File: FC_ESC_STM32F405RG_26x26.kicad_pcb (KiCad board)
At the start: 2 copper layers, 34 x 34 mm, 223 parts, among them J1 USB, J10 UART4, J11 PWM, J12 OSD, J13 ALARM, J14 LED_STRIP, J15 RC, J16 MOTOR, J17 MOTOR, J18 MOTOR, J19 MOTOR, J2 ESC_PROG, J21 Conn_02x03_Odd_Even, J22 Conn_02x02_Odd_Even, J3 Debugger, J4 VOL_CUR, J5 RSSI, J6 I2C2_UART3, J7 SD CARD, J8 UART1, J9 UART6, Q1 SIZ200, Q10 SIZ200, Q11 SIZ200, Q12 SIZ200, Q2 SIZ200, Q3 SIZ200, Q4 SIZ200, Q5 SIZ200, Q6 SIZ200, Q7 SIZ200, Q8 SIZ200, Q9 SIZ200, SW1 RST, U1 EFM8BB21, U10 FD6288Q, U11 outline, U12 MPU-6000, U13 BMP280, U14 LM358, U15 STM32F405RGTx, U16 TPS54331D, U2 EFM8BB21, U3 TPS54560BDDA, U4 FD6288Q, U5 FD6288Q, U7 EFM8BB21, U8 EFM8BB21, U9 FD6288Q, Y1 8MHz

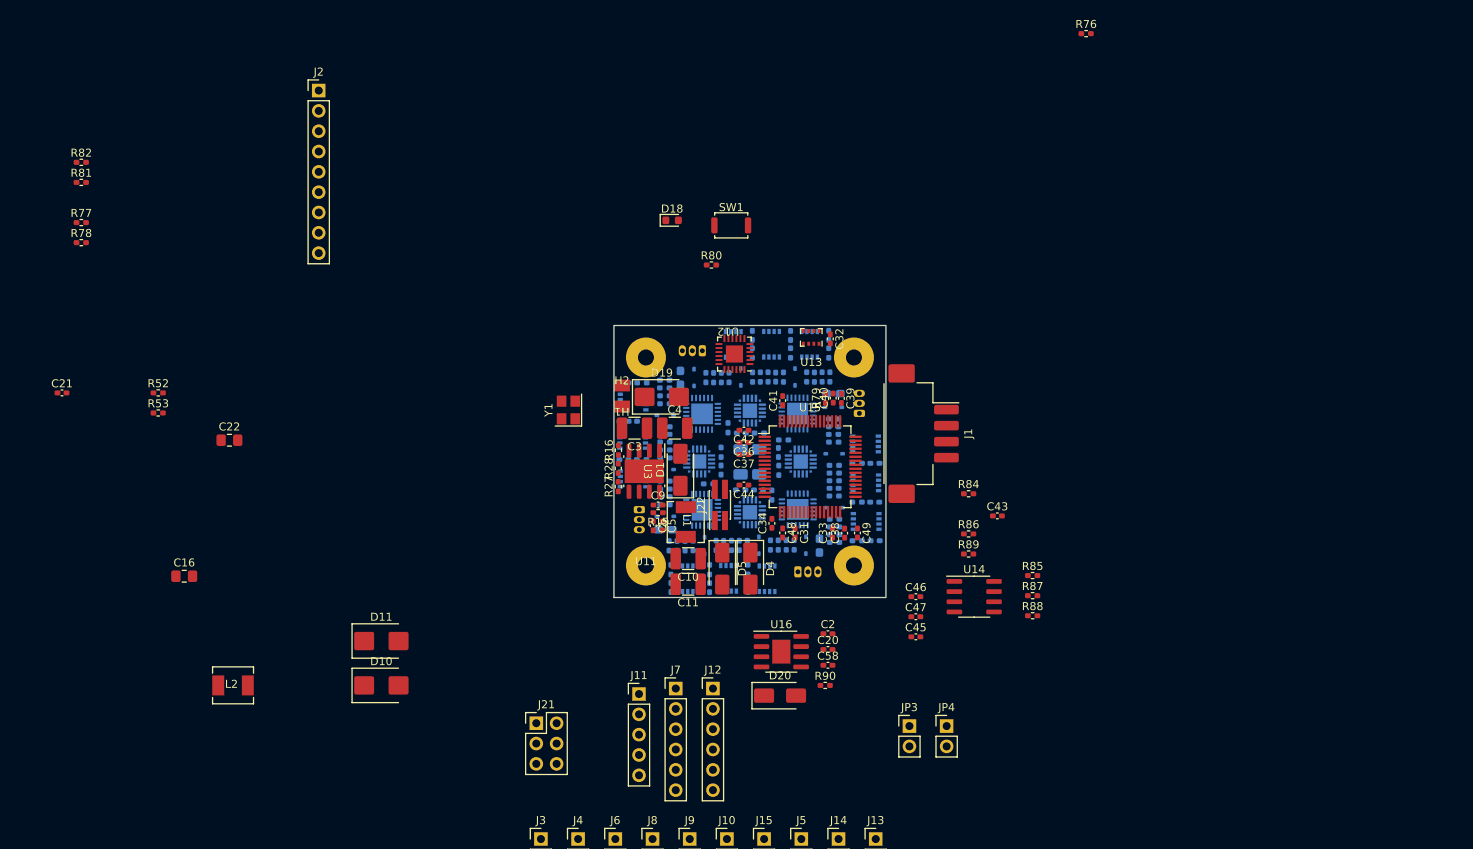
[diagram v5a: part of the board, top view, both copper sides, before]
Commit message: update placement
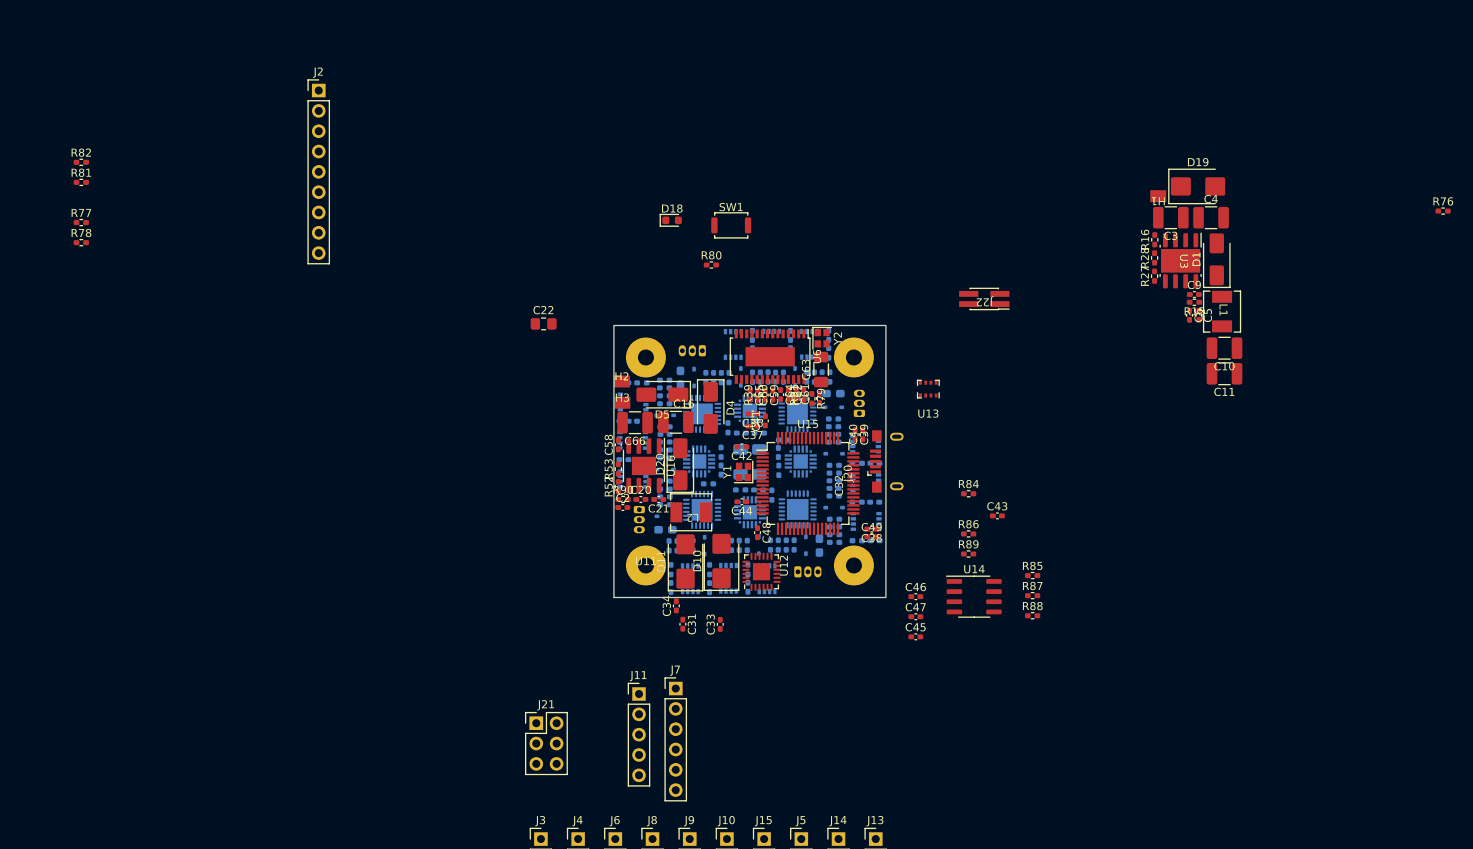
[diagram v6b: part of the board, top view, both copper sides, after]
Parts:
- removed J1: USB, Connector_Hirose:Hirose_DF3EA-04P-2H_1x04-1MP_P2.00mm_Horizontal
- removed J12: OSD, Connector_PinHeader_2.54mm:PinHeader_1x06_P2.54mm_Vertical
- removed JP3: Jumper_3V3_FC, Connector_PinHeader_2.54mm:PinHeader_1x02_P2.54mm_Vertical
- removed JP4: Jumper_3V3_ESC, Connector_PinHeader_2.54mm:PinHeader_1x02_P2.54mm_Vertical
- added C59: 100nF, Capacitor_SMD:C_0402_1005Metric_Pad0.74x0.62mm_HandSolder, F.Cu at (217.5, 71.9)
- added C60: 100nF, Capacitor_SMD:C_0402_1005Metric_Pad0.74x0.62mm_HandSolder, F.Cu at (218.4, 71.9)
- added C61: 47uF, Capacitor_SMD:C_0402_1005Metric_Pad0.74x0.62mm_HandSolder, F.Cu at (221.3, 71.8)
- added C62: 22uF, Capacitor_SMD:C_0402_1005Metric_Pad0.74x0.62mm_HandSolder, F.Cu at (220.4, 71.9)
- added C63: 4.7uF, Capacitor_SMD:C_1206_3216Metric_Pad1.33x1.80mm_HandSolder, F.Cu at (224.5, 68.7)
- added C64: 100nF, Capacitor_SMD:C_0402_1005Metric_Pad0.74x0.62mm_HandSolder, F.Cu at (219.4, 71.9)
- added C65: 100nF, Capacitor_SMD:C_0402_1005Metric_Pad0.74x0.62mm_HandSolder, F.Cu at (215.6, 71.9)
- added C66: 10uF, Capacitor_SMD:C_1210_3225Metric_Pad1.33x2.70mm_HandSolder, F.Cu at (201.2, 75.4)
- added H3: Pad_5V_IN, Proj_footprint:MoutingPad, F.Cu at (199.6, 72.9)
- added J20: USB_A, Proj_footprint:USB_Micro-B_2P_4hole, F.Cu at (236.1, 80.2)
- added R39: 75R, Resistor_SMD:R_0402_1005Metric_Pad0.72x0.64mm_HandSolder, F.Cu at (216.5, 71.9)
- added R91: 75R, Resistor_SMD:R_0402_1005Metric_Pad0.72x0.64mm_HandSolder, F.Cu at (222.3, 71.9)
- added U6: AT7456, Package_SO:TSSOP-28-1EP_4.4x9.7mm_P0.65mm, F.Cu at (218.1, 67.1)
- added Y2: 8Mhz, Crystal:Crystal_SMD_2016-4Pin_2.0x1.6mm, F.Cu at (224.6, 64.8)
- C16: footprint Capacitor_SMD:C_0805_2012Metric_Pad1.18x1.45mm_HandSolder -> Capacitor_SMD:C_1210_3225Metric_Pad1.33x2.70mm_HandSolder
- J22: footprint Connector_PinHeader_1.27mm:PinHeader_2x02_P1.27mm_Vertical_SMD -> Proj_footprint:PinHeader_2x02_P1.27mm_Vertical_SMD
- Y1: footprint Crystal:Crystal_SMD_3225-4Pin_3.2x2.5mm -> Crystal:Crystal_SMD_2016-4Pin_2.0x1.6mm
- moved C21 75.8 mm to (204.2, 85.0), turned to 180 degrees
- moved D1 72.0 mm to (273.9, 55.0)
- moved H1 72.0 mm to (266.6, 47.1)
- moved R27 72.0 mm to (266.1, 57.1)
- moved R28 72.0 mm to (266.1, 54.8)
- moved C10 72.0 mm to (274.9, 66.1)
- moved C11 72.0 mm to (274.9, 69.3)
- moved C3 72.0 mm to (268.2, 49.8)
- moved C4 72.0 mm to (273.2, 49.8)
- moved C5 72.0 mm to (271.7, 62.0)
- moved L1 72.0 mm to (274.6, 61.5)
- moved R16 72.0 mm to (266.2, 52.5)
- moved U3 72.0 mm to (269.4, 55.1)
- moved C6 72.0 mm to (270.5, 62.0)
- moved D19 72.0 mm to (271.6, 45.9)
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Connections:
- net BARO_CLK renamed SPI3_CLK
- net BARO_MISO renamed SPI3_MISO
- net BARO_MOSI renamed SPI3_MOSI
- C16 pad 1: Net-(J22-Pin_4) -> +5V
- D4 pad 1: Net-(D4-K) -> +5V
- D5 pad 1: Net-(D4-K) -> +5V
- J22 pad 1: Net-(D4-K) -> Net-(D10-K)
- J22 pad 2: +5V -> 3V3_FC
- J22 pad 3: Net-(D4-K) -> Net-(D10-K)
- J22 pad 4: Net-(J22-Pin_4) -> 3V3_ESC
- U16 pad 2: Net-(J22-Pin_4) -> +5V

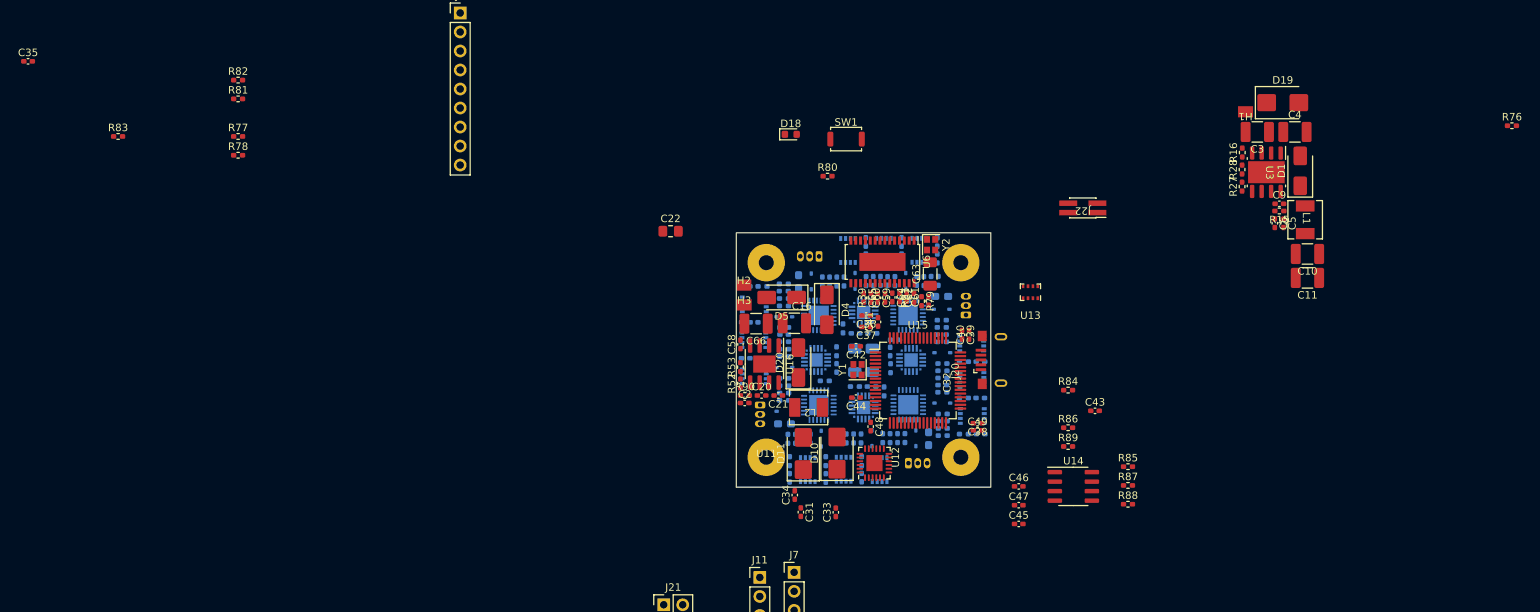
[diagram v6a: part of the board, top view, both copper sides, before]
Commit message: update placement
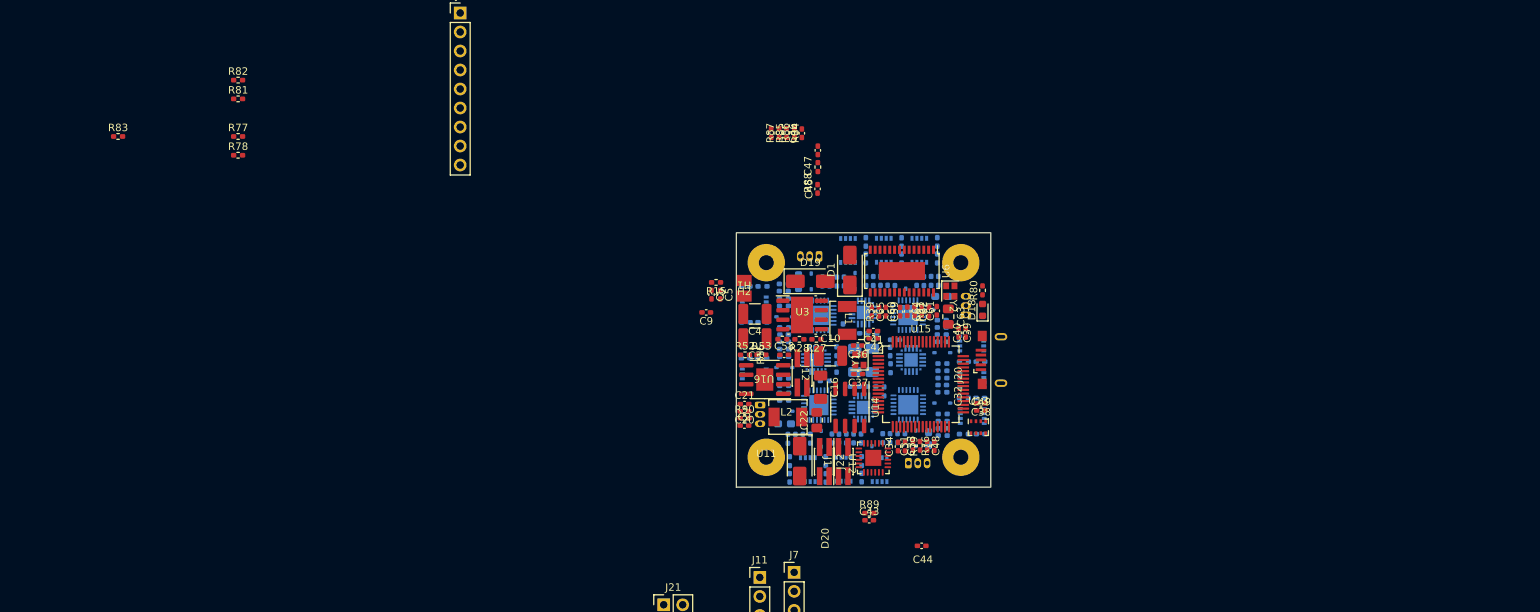
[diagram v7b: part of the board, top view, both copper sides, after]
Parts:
- removed C11, C66: 10uF, Capacitor_SMD:C_1210_3225Metric_Pad1.33x2.70mm_HandSolder
- removed C35: 100nF, Capacitor_SMD:C_0402_1005Metric_Pad0.74x0.62mm_HandSolder
- removed D10, D11: SS24, Diode_SMD:D_SMB
- removed D4, D5: SS34, Diode_SMD:D_SMA
- removed H3: Pad_5V_IN, Proj_footprint:MoutingPad
- removed SW1: RST, Button_Switch_SMD:SW_Push_SPST_NO_Alps_SKRK
- added J1: Conn_02x02_Odd_Even, Proj_footprint:PinHeader_2x02_P1.27mm_Vertical_SMD, F.Cu at (210.2, 93.8)
- added J12: Conn_02x02_Odd_Even, Proj_footprint:PinHeader_2x02_P1.27mm_Vertical_SMD, F.Cu at (207.3, 82.0)
- C16: footprint Capacitor_SMD:C_1210_3225Metric_Pad1.33x2.70mm_HandSolder -> Capacitor_SMD:C_1206_3216Metric_Pad1.33x1.80mm_HandSolder
- C4: value 10uF -> 100uF
- C63: footprint Capacitor_SMD:C_1206_3216Metric_Pad1.33x1.80mm_HandSolder -> Capacitor_SMD:C_0805_2012Metric_Pad1.18x1.45mm_HandSolder
- D19: value SS54 -> SS34; footprint Diode_SMD:D_SMB -> Diode_SMD:D_SMA
- U16: footprint Package_SO:SOIC-8-1EP_3.9x4.9mm_P1.27mm_EP2.29x3mm -> Proj_footprint:SOIC-8-1EP_3.9x4.9mm_P1.27mm_EP2.29x3mm
- Y1, Y2: footprint Crystal:Crystal_SMD_2016-4Pin_2.0x1.6mm -> Proj_footprint:Crystal_SMD_2016-4Pin_2.0x1.6mm
- moved R76 88.3 mm to (225.0, 91.7), turned to 90 degrees
- moved C9 77.9 mm to (194.5, 73.9), turned to 180 degrees
- moved C4 76.1 mm to (201.0, 74.1), turned to 180 degrees
- moved C5 75.9 mm to (196.4, 71.5)
- moved C6 75.9 mm to (195.2, 71.5)
- moved R15 75.9 mm to (195.8, 69.9)
- moved C3 72.6 mm to (201.0, 77.3)
- moved H1 70.7 mm to (199.6, 69.6)
- moved D19 67.5 mm to (208.4, 69.7)
- moved R16 66.3 mm to (204.7, 77.4), turned to 180 degrees
- moved R87 66.3 mm to (204.3, 49.9), turned to 90 degrees
- moved R85 65.3 mm to (203.2, 49.9), turned to -90 degrees
- moved C10 65.2 mm to (211.1, 79.7), turned to 0 degrees
- moved U3 64.9 mm to (207.3, 74.2), turned to 0 degrees
- moved R28 63.4 mm to (207.0, 77.5), turned to 180 degrees
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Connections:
- C1 pad 2: GND -> +5V
- C10 pad 1: Net-(D5-A) -> Net-(J12-Pin_3)
- C10 pad 2: GND -> +5V
- C16 pad 1: +5V -> Net-(J12-Pin_3)
- C16 pad 2: GND -> +5V
- C19 pad 2: GND -> +5V
- C2 pad 2: GND -> +5V
- C20 pad 2: GND -> +5V
- C22 pad 2: GND -> +5V
- C23 pad 2: GND -> +5V
- C24 pad 2: GND -> +5V
- C3 pad 2: GND -> +5V
- C31 pad 2: GND -> +5V
- C32 pad 2: GND -> +5V
- C33 pad 2: GND -> +5V
- C34 pad 2: GND -> +5V
- C36 pad 2: GND -> +5V
- C37 pad 2: GND -> +5V
- C38 pad 1: GND -> +5V
- C39 pad 1: GND -> +5V
- C4 pad 2: GND -> +5V
- C40 pad 2: GND -> +5V
- C41 pad 2: GND -> +5V
- C42 pad 2: GND -> +5V
- C43 pad 2: GND -> +5V
- C44 pad 2: GND -> +5V
- C45 pad 2: GND -> +5V
- C46 pad 2: GND -> +5V
- C47 pad 2: GND -> +5V
- C48 pad 2: GND -> +5V
- C49 pad 2: GND -> +5V
- C5 pad 2: GND -> +5V
- C50 pad 2: GND -> +5V
- C51 pad 2: GND -> +5V
- C52 pad 2: GND -> +5V
- C53 pad 2: GND -> +5V
- C54 pad 2: GND -> +5V
- C55 pad 2: GND -> +5V
- C56 pad 2: GND -> +5V
- C57 pad 2: GND -> +5V
- C58 pad 2: GND -> +5V
- C59 pad 2: GND -> +5V
- C6 pad 2: GND -> +5V
- C63 pad 2: GND -> +5V
- C64 pad 2: GND -> +5V
- C65 pad 2: GND -> +5V
- C7 pad 2: GND -> +5V
- C8 pad 2: GND -> +5V
- D1 pad 2: GND -> +5V
- D19 pad 2: GND -> +5V
- D20 pad 2: GND -> +5V
- H2 pad 1: GND -> +5V
- J10 pad 4: GND -> +5V
- J11 pad 5: GND -> +5V
- J13 pad 3: GND -> +5V
- J14 pad 3: GND -> +5V
- J15 pad 3: GND -> +5V
- J2 pad 9: GND -> +5V
- J20 pad 4: GND -> +5V
- J20 pad 5: GND -> +5V
- J21 pad 5: GND -> +5V
- J21 pad 6: GND -> +5V
- J3 pad 4: GND -> +5V
- J4 pad 4: GND -> +5V
- J5 pad 3: GND -> +5V
- J6 pad 4: GND -> +5V
- J7 pad 6: GND -> +5V
- J8 pad 4: GND -> +5V
- J9 pad 4: GND -> +5V
- L1 pad 2: Net-(D5-A) -> Net-(J12-Pin_3)
- Q1 pad 1: GND -> +5V
- Q10 pad 1: GND -> +5V
- Q11 pad 1: GND -> +5V
- Q12 pad 1: GND -> +5V
- Q2 pad 1: GND -> +5V
- Q3 pad 1: GND -> +5V
- Q4 pad 1: GND -> +5V
- Q5 pad 1: GND -> +5V
- Q6 pad 1: GND -> +5V
- Q7 pad 1: GND -> +5V
- Q8 pad 1: GND -> +5V
- Q9 pad 1: GND -> +5V
- R13 pad 1: GND -> +5V
- R14 pad 1: GND -> +5V
- R16 pad 2: GND -> +5V
- R25 pad 1: GND -> +5V
- R26 pad 1: GND -> +5V
- R27 pad 1: Net-(D5-A) -> Net-(J12-Pin_3)
- R28 pad 2: GND -> +5V
- R37 pad 1: GND -> +5V
- R38 pad 1: GND -> +5V
- R39 pad 2: GND -> +5V
- R53 pad 2: GND -> +5V
- R54 pad 1: GND -> +5V
- R55 pad 1: GND -> +5V
- R64 pad 1: GND -> +5V
- R65 pad 1: GND -> +5V
- R74 pad 1: GND -> +5V
- R75 pad 1: GND -> +5V
- R78 pad 2: GND -> +5V
- R84 pad 1: GND -> +5V
- R85 pad 1: GND -> +5V
- U1 pad 12: GND -> +5V
- U1 pad 21: GND -> +5V
- U1 pad 3: GND -> +5V
- U10 pad 6: GND -> +5V
- U12 pad 1: GND -> +5V
- U12 pad 11: GND -> +5V
- U12 pad 18: GND -> +5V
- U13 pad 1: GND -> +5V
- U13 pad 7: GND -> +5V
- U14 pad 4: GND -> +5V
- U15 pad 12: GND -> +5V
- U15 pad 18: GND -> +5V
- U15 pad 63: GND -> +5V
- U16 pad 7: GND -> +5V
- U2 pad 12: GND -> +5V
- U2 pad 21: GND -> +5V
- U2 pad 3: GND -> +5V
- U3 pad 7: GND -> +5V
- U3 pad 9: GND -> +5V
- U4 pad 6: GND -> +5V
- U5 pad 6: GND -> +5V
- U6 pad 20: GND -> +5V
- U6 pad 23: GND -> +5V
- U6 pad 4: GND -> +5V
- U7 pad 12: GND -> +5V
- U7 pad 21: GND -> +5V
- U7 pad 3: GND -> +5V
- U8 pad 12: GND -> +5V
- U8 pad 21: GND -> +5V
- U8 pad 3: GND -> +5V
- U9 pad 6: GND -> +5V
